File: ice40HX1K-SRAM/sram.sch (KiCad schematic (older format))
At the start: 3 parts

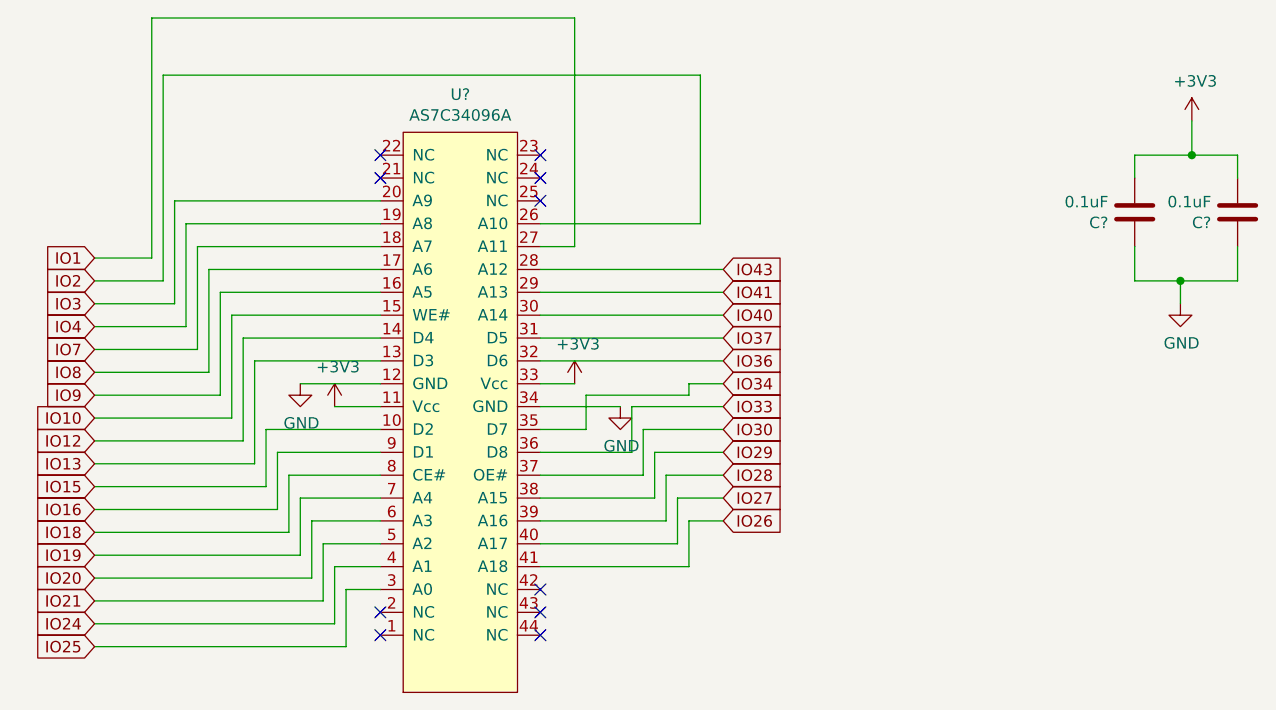
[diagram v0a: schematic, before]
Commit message: wiring FPGA nRF52 and ATSAMD11
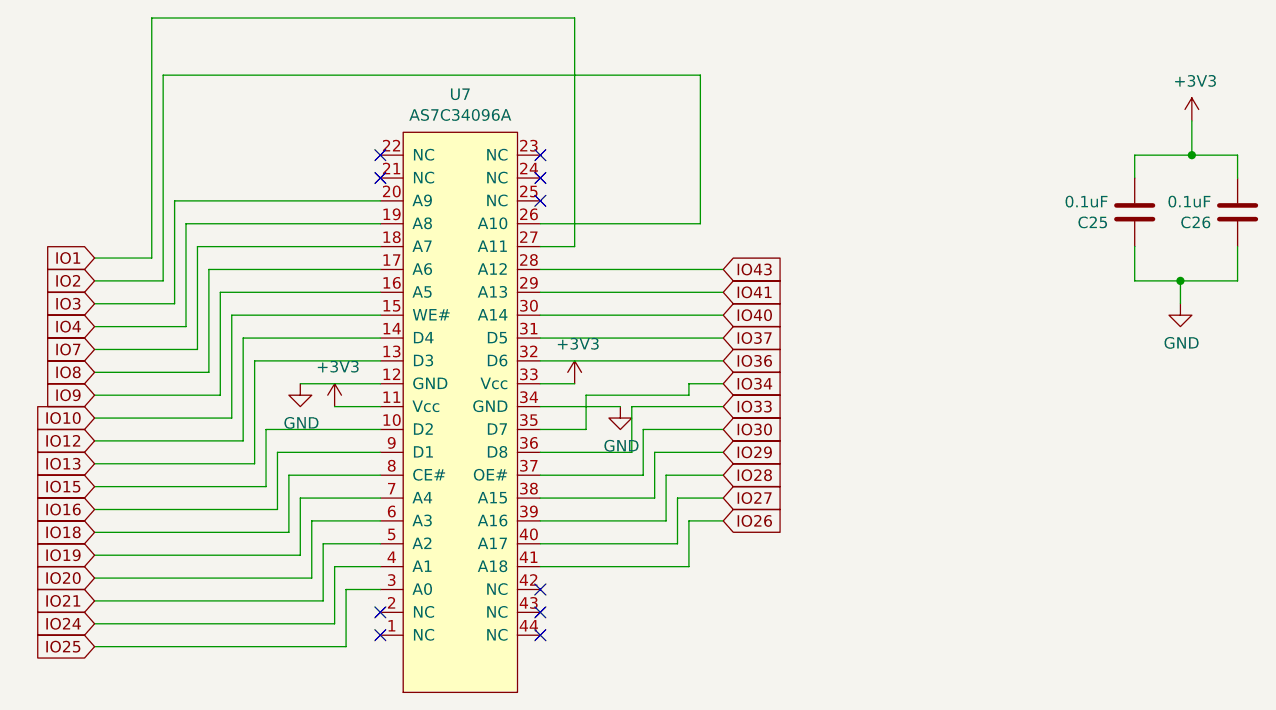
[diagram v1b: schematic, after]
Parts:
- gave numbers to parts that had none: 3
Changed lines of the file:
@@
 P 3100 4300
 AR Path="/5E66A7AA" Ref="U?"  Part="1"
-AR Path="/5E6627F3/5E66A7AA" Ref="U?"  Part="1"
-F 0 "U?" H 3100 1885 50  0000 C CNN
+AR Path="/5E6627F3/5E66A7AA" Ref="U7"  Part="1"
+F 0 "U7" H 3100 1885 50  0000 C CNN
 F 1 "AS7C34096A" H 3100 1976 50  0000 C CNN
 F 2 "Package_SO:TSOP-II-44_10.16x18.41mm_P0.8mm" H 3100 4300 50  0001 C CNN
@@
 P 2400 3150
 AR Path="/5E66A7B5" Ref="#PWR?"  Part="1"
-AR Path="/5E6627F3/5E66A7B5" Ref="#PWR?"  Part="1"
-F 0 "#PWR?" H 2400 2900 50  0001 C CNN
+AR Path="/5E6627F3/5E66A7B5" Ref="#PWR045"  Part="1"
+F 0 "#PWR045" H 2400 2900 50  0001 C CNN
 F 1 "GND" H 2405 2977 50  0000 C CNN
 F 2 "" H 2400 3150 50  0001 C CNN
@@
 P 3800 3250
 AR Path="/5E66A7BB" Ref="#PWR?"  Part="1"
-AR Path="/5E6627F3/5E66A7BB" Ref="#PWR?"  Part="1"
-F 0 "#PWR?" H 3800 3000 50  0001 C CNN
+AR Path="/5E6627F3/5E66A7BB" Ref="#PWR048"  Part="1"
+F 0 "#PWR048" H 3800 3000 50  0001 C CNN
 F 1 "GND" H 3805 3077 50  0000 C CNN
 F 2 "" H 3800 3250 50  0001 C CNN
@@
 P 3600 3150
 AR Path="/5E66A7C1" Ref="#PWR?"  Part="1"
-AR Path="/5E6627F3/5E66A7C1" Ref="#PWR?"  Part="1"
-F 0 "#PWR?" H 3600 3000 50  0001 C CNN
+AR Path="/5E6627F3/5E66A7C1" Ref="#PWR047"  Part="1"
+F 0 "#PWR047" H 3600 3000 50  0001 C CNN
 F 1 "+3V3" H 3615 3323 50  0000 C CNN
 F 2 "" H 3600 3150 50  0001 C CNN
@@
 P 2550 3250
 AR Path="/5E66A7C7" Ref="#PWR?"  Part="1"
-AR Path="/5E6627F3/5E66A7C7" Ref="#PWR?"  Part="1"
-F 0 "#PWR?" H 2550 3100 50  0001 C CNN
+AR Path="/5E6627F3/5E66A7C7" Ref="#PWR046"  Part="1"
+F 0 "#PWR046" H 2550 3100 50  0001 C CNN
 F 1 "+3V3" H 2565 3423 50  0000 C CNN
 F 2 "" H 2550 3250 50  0001 C CNN
@@
 AR Path="/5E6179A9" Ref="C?"  Part="1"
 AR Path="/5E5F7D61/5E6179A9" Ref="C?"  Part="1"
-AR Path="/5E6627F3/5E6179A9" Ref="C?"  Part="1"
-F 0 "C?" H 6165 2446 50  0000 L CNN
+AR Path="/5E6627F3/5E6179A9" Ref="C25"  Part="1"
+F 0 "C25" H 6165 2446 50  0000 L CNN
 F 1 "0.1uF" H 6165 2355 50  0000 L CNN
 F 2 "Capacitor_SMD:C_0805_2012Metric" H 6088 2250 50  0001 C CNN
@@
 AR Path="/5E6179AF" Ref="C?"  Part="1"
 AR Path="/5E5F7D61/5E6179AF" Ref="C?"  Part="1"
-AR Path="/5E6627F3/5E6179AF" Ref="C?"  Part="1"
-F 0 "C?" H 6615 2446 50  0000 L CNN
+AR Path="/5E6627F3/5E6179AF" Ref="C26"  Part="1"
+F 0 "C26" H 6615 2446 50  0000 L CNN
 F 1 "0.1uF" H 6615 2355 50  0000 L CNN
 F 2 "Capacitor_SMD:C_0805_2012Metric" H 6538 2250 50  0001 C CNN
@@
 AR Path="/5E6179B5" Ref="#PWR?"  Part="1"
 AR Path="/5E5F7D61/5E6179B5" Ref="#PWR?"  Part="1"
-AR Path="/5E6627F3/5E6179B5" Ref="#PWR?"  Part="1"
-F 0 "#PWR?" H 6250 2550 50  0001 C CNN
+AR Path="/5E6627F3/5E6179B5" Ref="#PWR049"  Part="1"
+F 0 "#PWR049" H 6250 2550 50  0001 C CNN
 F 1 "GND" H 6255 2627 50  0000 C CNN
 F 2 "" H 6250 2800 50  0001 C CNN
@@
 AR Path="/5E6179BB" Ref="#PWR?"  Part="1"
 AR Path="/5E5F7D61/5E6179BB" Ref="#PWR?"  Part="1"
-AR Path="/5E6627F3/5E6179BB" Ref="#PWR?"  Part="1"
-F 0 "#PWR?" H 6300 1850 50  0001 C CNN
+AR Path="/5E6627F3/5E6179BB" Ref="#PWR050"  Part="1"
+F 0 "#PWR050" H 6300 1850 50  0001 C CNN
 F 1 "+3V3" H 6315 2173 50  0000 C CNN
 F 2 "" H 6300 2000 50  0001 C CNN

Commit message: wiring FPGA
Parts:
- C25, C26: footprint Capacitor_SMD:C_0805_2012Metric -> Capacitor_SMD:C_0402_1005Metric
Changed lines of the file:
@@
 F 0 "C25" H 6165 2446 50  0000 L CNN
 F 1 "0.1uF" H 6165 2355 50  0000 L CNN
-F 2 "Capacitor_SMD:C_0805_2012Metric" H 6088 2250 50  0001 C CNN
+F 2 "Capacitor_SMD:C_0402_1005Metric" H 6088 2250 50  0001 C CNN
 F 3 "~" H 6050 2400 50  0001 C CNN
 	1    6050 2400
@@
 F 0 "C26" H 6615 2446 50  0000 L CNN
 F 1 "0.1uF" H 6615 2355 50  0000 L CNN
-F 2 "Capacitor_SMD:C_0805_2012Metric" H 6538 2250 50  0001 C CNN
+F 2 "Capacitor_SMD:C_0402_1005Metric" H 6538 2250 50  0001 C CNN
 F 3 "~" H 6500 2400 50  0001 C CNN
 	1    6500 2400
